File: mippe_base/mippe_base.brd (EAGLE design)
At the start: 160 x 100 mm, 17 parts, among them IC1 ATMEGA168PROUND, SW1 BTN-PTS810

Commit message: Finish burnin and mippe controller
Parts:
- added D2: RED, scono:LED-0603
- added J8: (no value), scono:1X04_NO_SILK
- added J9: BURNIN, scono:BURNIN
- added R3: 330R, scono:R0603
- R2: value (none) -> 330R
- Y1: value (none) -> 16MHz
- moved J3 13.7 mm to (20.3, 48.3)
- moved J4 13.7 mm to (20.3, 45.7)
- moved J2 13.7 mm to (20.3, 10.2)
- moved J5 13.7 mm to (20.3, 40.6)
- moved J6 13.7 mm to (20.3, 35.6)
- moved J1 9.96 mm to (5.08, 51.2)
- moved C1 7.62 mm to (8.10, 24.3)
- moved C2 7.62 mm to (19.7, 22.8)
- moved D1 7.62 mm to (4.18, 32.4)
- moved C3 7.62 mm to (3.38, 28.0)
- moved C4 7.62 mm to (3.38, 10.0)
- moved R2 7.62 mm to (5.95, 32.5)
- moved Y1 7.62 mm to (3.38, 19.0)
- moved R1 7.62 mm to (8.05, 43.1)
- moved SW1 7.62 mm to (9.87, 46.2)
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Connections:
- removed net DTR: J1.6
- new net N$2: D2.A, R3.2
- net 3.3V: now also J9.3.3V, R3.1
- net GND: now also D2.C, J9.GND
- net GPIO3: now also J8.4
- net GPIO4: now also J8.3
- net GPIO5: now also J8.2
- net GPIO6: now also J8.1
- net MISO: now also J9.MISO
- net MOSI: now also J9.MOSI
- net RST: now also J1.6
- net SCK: now also J9.SCK
- net SS: now also J9.SS
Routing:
- net MISO: track 0.00 -> 24.9 mm, vias 0 -> 1
- net SCK: track 0.00 -> 22.7 mm, vias 0 -> 1
- net TX: track 0.00 -> 20.8 mm
- net RST: track 0.00 -> 19.9 mm, vias 0 -> 1
- net GND: track 0.00 -> 19.4 mm, vias 0 -> 5
- net RX: track 0.00 -> 18.1 mm
- net MOSI: track 0.00 -> 14.7 mm
- net SS: track 0.00 -> 13.6 mm
- net N$4: track 0.00 -> 12.9 mm
- net N$3: track 0.00 -> 12.7 mm
- net GPIO0: track 0.00 -> 4.30 mm
- net 3.3V: track 0.00 -> 4.04 mm, vias 0 -> 1
- net ADC3: track 0.00 -> 2.65 mm
- net ADC1: track 0.00 -> 2.60 mm
- net SDA: track 0.00 -> 2.60 mm
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- added copper zone on layer 1, net 3.3V
- added copper zone on layer 16, net GND
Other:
- board size 160 x 100 mm -> 22.9 x 53.3 mm
- board text added: "3V3"
- board text added: "ADC"
- board text added: "Arduino Bootloader Burnin"
- board text added: "Arduino Uno Redesign Fa19"
- board text added: "Arias Research Group Seiya Ono"
- board text added: "GND"
- board text added: "I2C"
- board text added: "MIPPE"
- board text added: "SPI"
- board text added: "UART"
- board text added: "USB to TTL Interface"

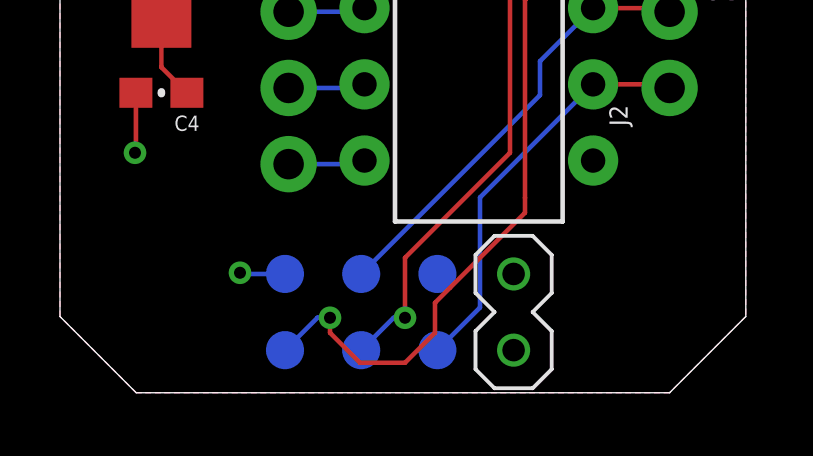
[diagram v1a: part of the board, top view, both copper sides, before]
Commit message: fix burnin OE and make QFP MIPPE
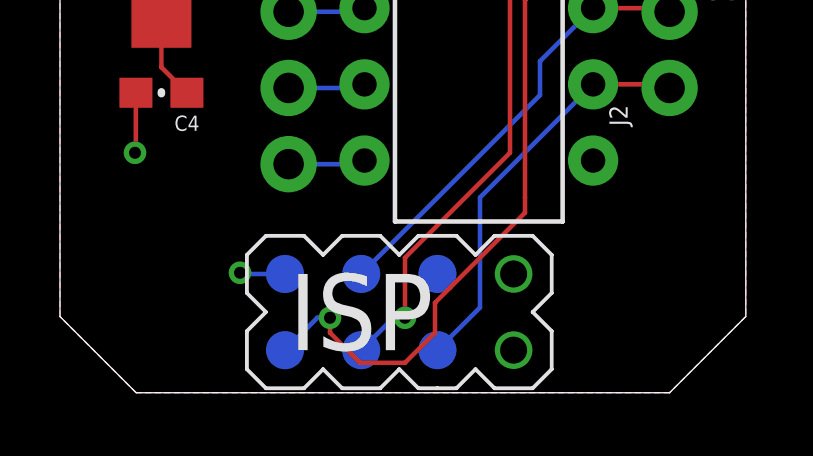
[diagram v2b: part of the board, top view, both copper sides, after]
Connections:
- net SS: now also J9.RST; no longer J9.SS
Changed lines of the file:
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@@
 <?xml version="1.0" encoding="utf-8"?>
 <!DOCTYPE eagle SYSTEM "eagle.dtd">
-<eagle version="9.4.2">
+<eagle version="9.5.0">
 <drawing>
 <settings>
@@
 <setting verticaltext="up"/>
 </settings>
-<grid distance="0.5" unitdist="mm" unit="mm" style="lines" multiple="1" display="yes" altdistance="5" altunitdist="mil" altunit="mil"/>
+<grid distance="0.25" unitdist="mm" unit="mm" style="lines" multiple="2" display="yes" altdistance="5" altunitdist="mil" altunit="mil"/>
 <layers>
 <layer number="1" name="Top" color="4" fill="1" visible="yes" active="yes"/>
@@
 <contactref element="IC1" pad="16"/>
 <contactref element="J2" pad="1"/>
-<contactref element="J9" pad="SS"/>
+<contactref element="J9" pad="RST"/>
 <wire x1="17.77" y1="10.28" x2="20.2" y2="10.28" width="0.1524" layer="1"/>
 <wire x1="20.2" y1="10.28" x2="20.32" y2="10.16" width="0.1524" layer="1"/>
